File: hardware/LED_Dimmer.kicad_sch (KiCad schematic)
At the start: 11 parts, among them J1 Molex PicoBlade 53261-0871 1x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, Q1 2N7002K-7, Q2 2N7002K-7, Q3 2N7002K-7, U1 BGM220P, U2 L78L33A

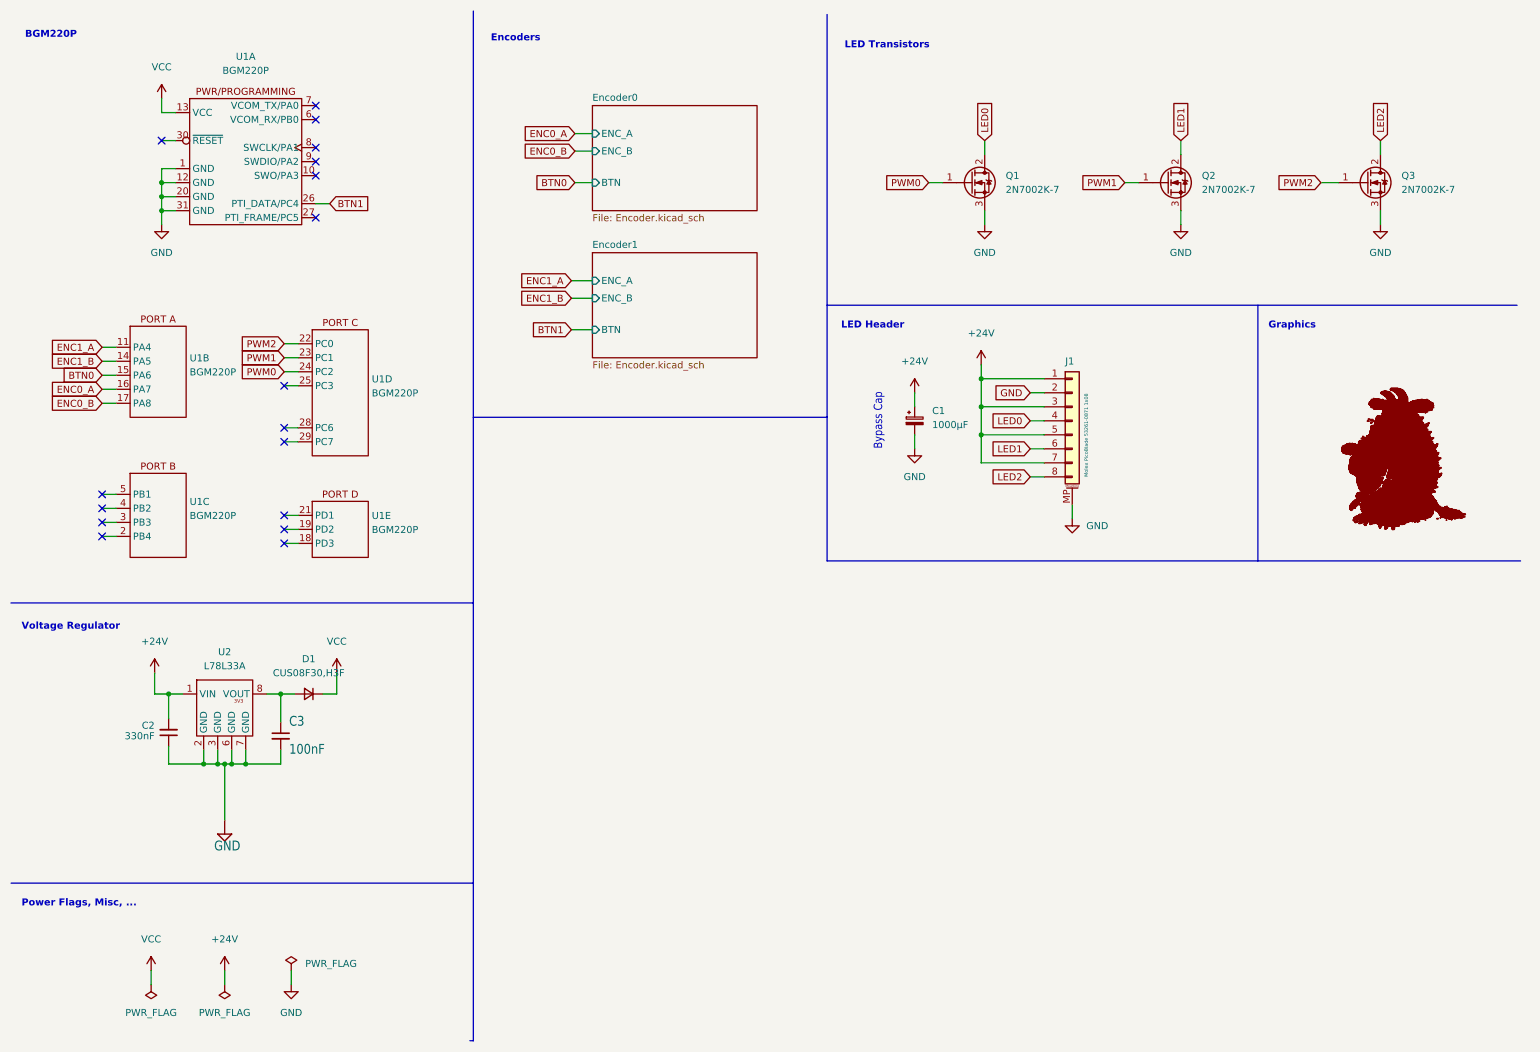
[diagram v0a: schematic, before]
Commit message: v2 Board Ready - Added Art - Removed DRC/ERC - Finished BOM
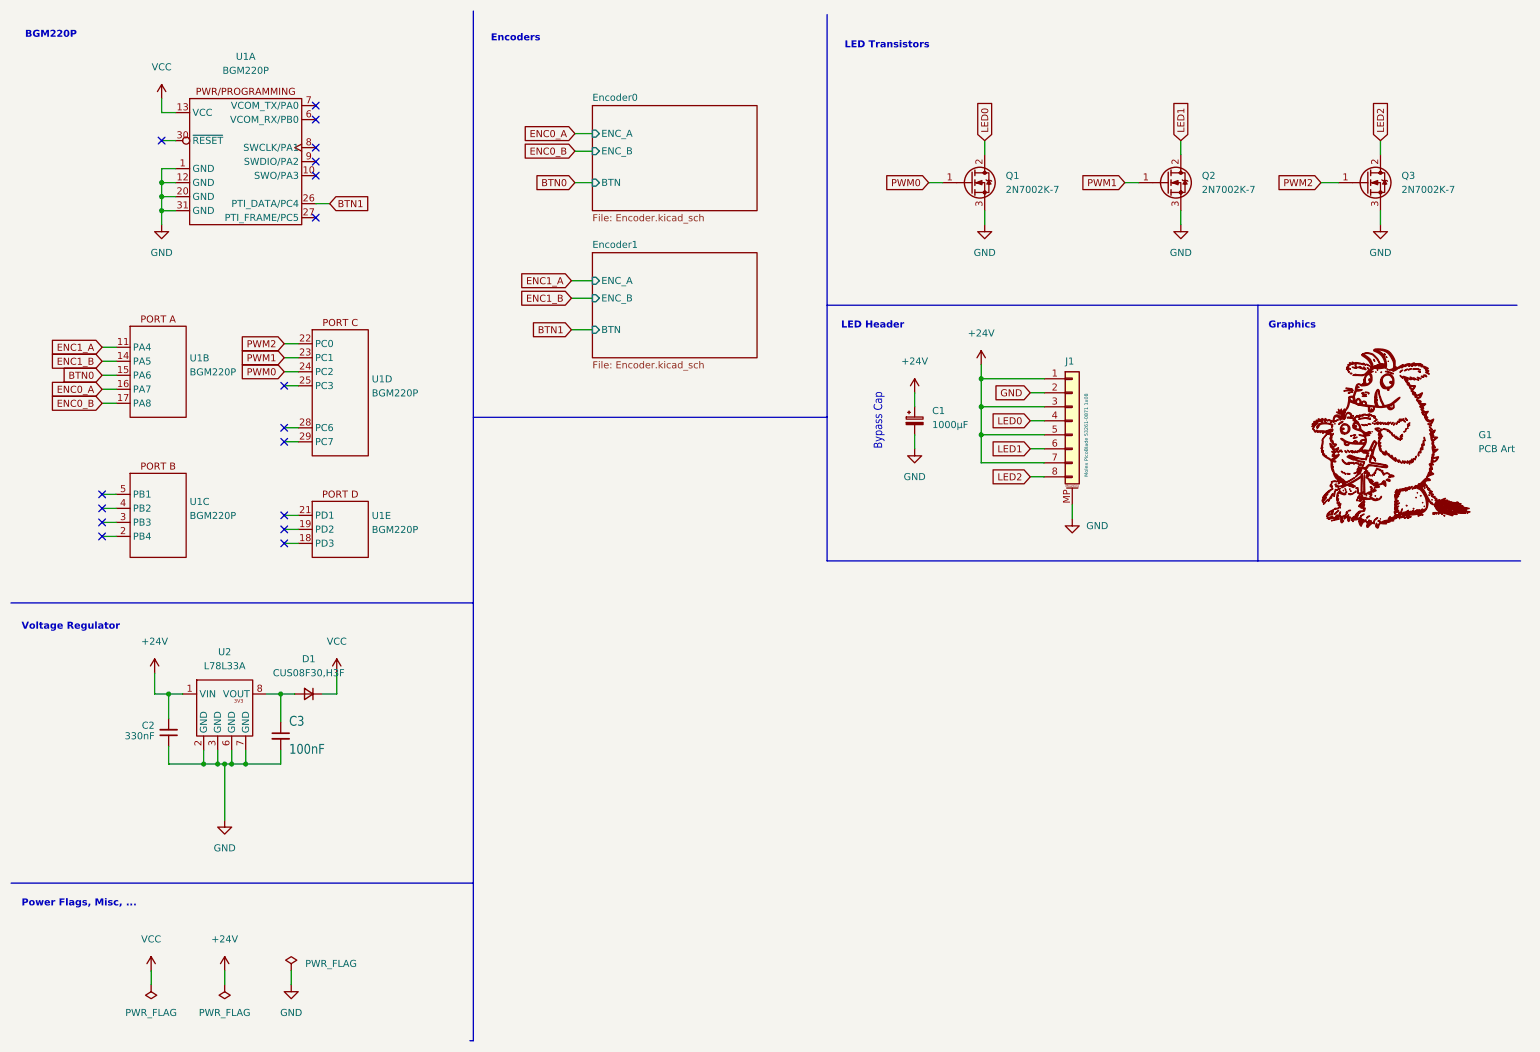
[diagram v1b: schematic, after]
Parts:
- removed G1: GRUFFALO, LED_Dimmer:GRUFFALO, symbol LED_Dimmer-eagle-import:GRUFFALO
- added G1: PCB Art, Gruffalo_Dimmer:Gruffalo_Art, symbol Gruffalo_Dimmer:PCB Art
- C3: Comments (none) -> Any X7R, 0603, 10V cap. Farnell MPN is alternative; Digikey PN (none) -> 1276-1935-1-ND; Farnell PN (none) -> 1362556; MPN (none) -> CL10B104KB8NNWC; Manufacturer (none) -> Samsung; Tolerance (none) -> X7R; Vrating (none) -> 50V

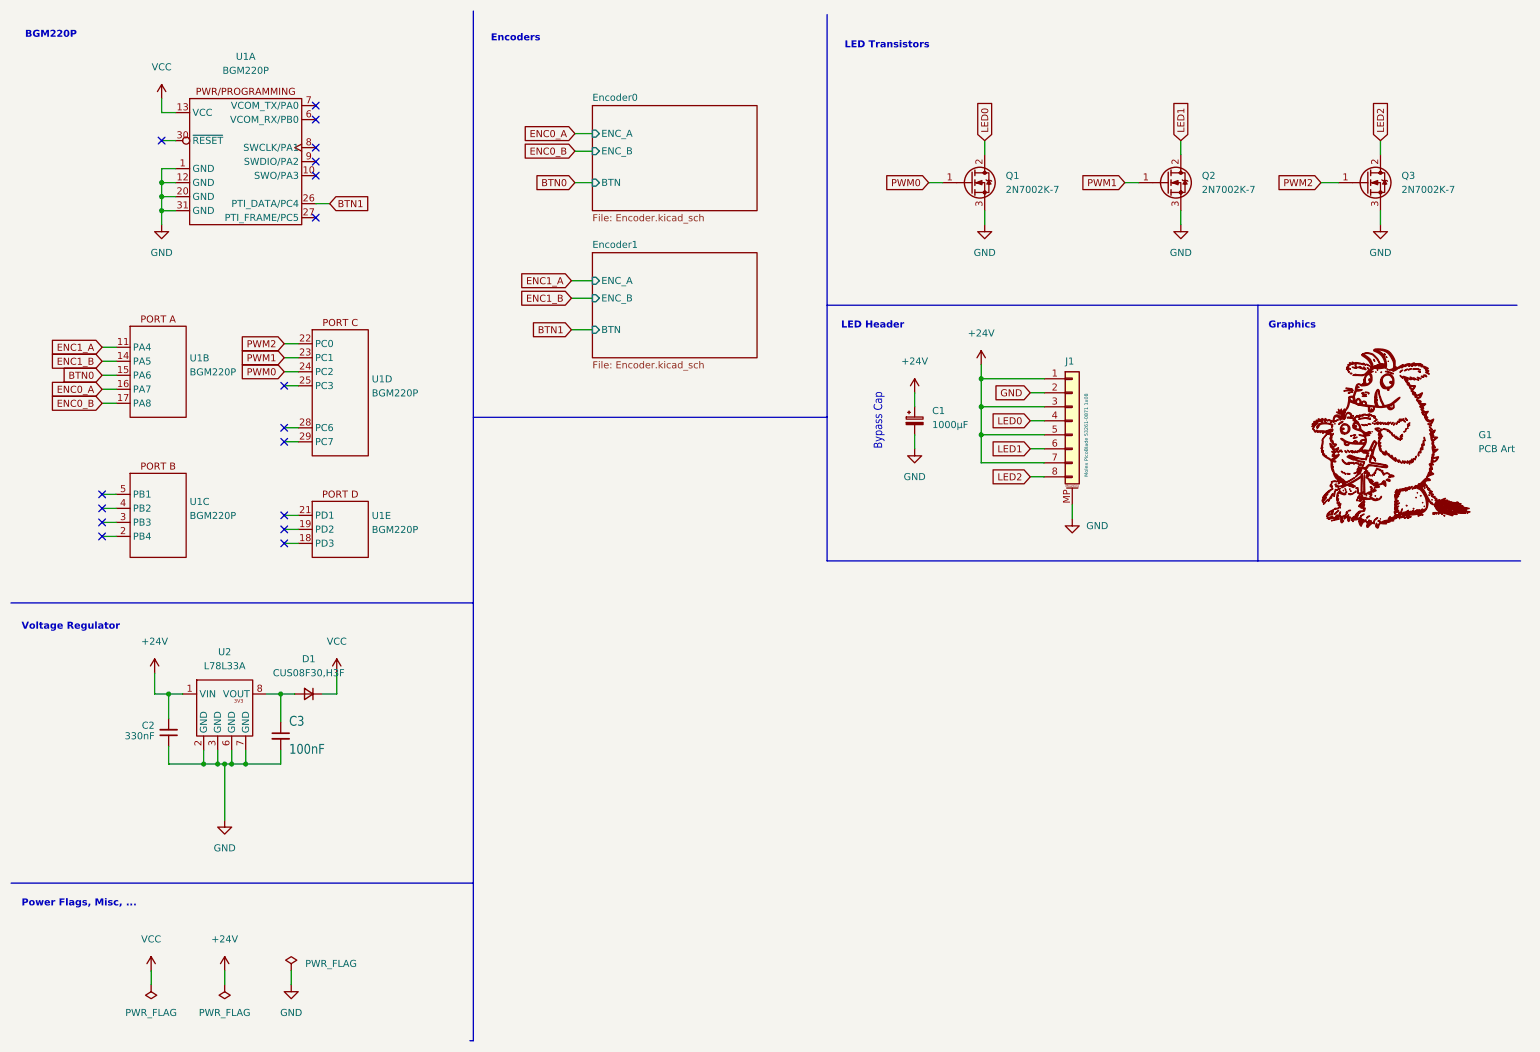
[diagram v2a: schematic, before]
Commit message: Not sure of the complete list of changes, but fixed a bunch of DRC/ERC errors
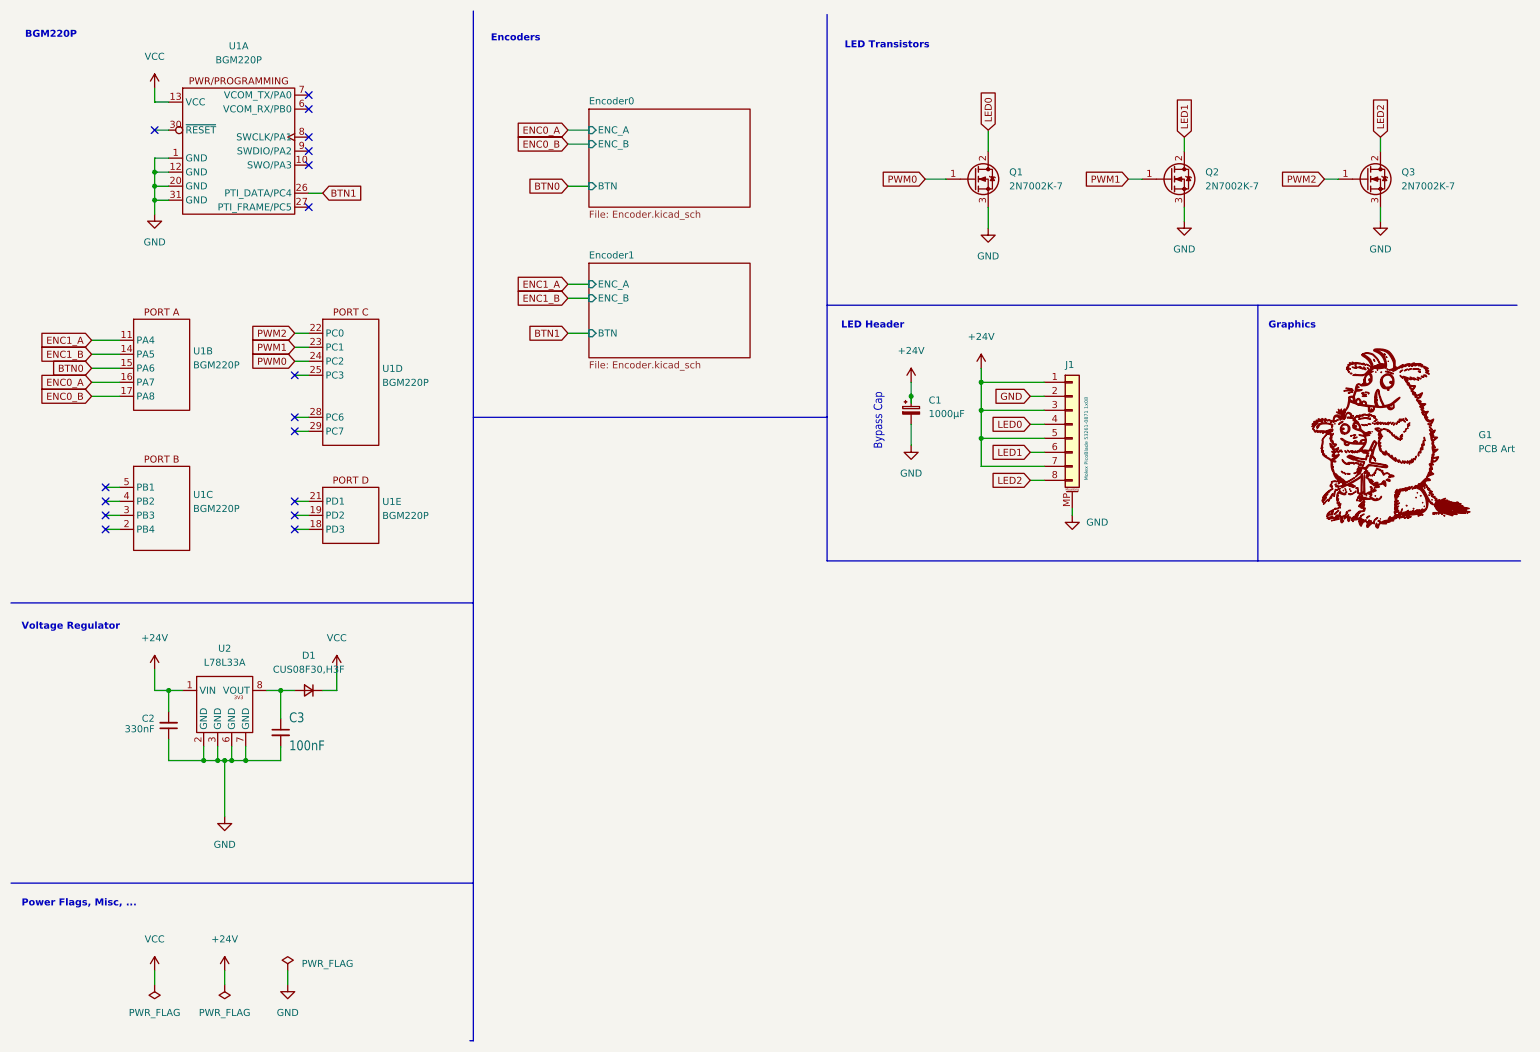
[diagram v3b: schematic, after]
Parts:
- G1: now left out of the parts list
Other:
- moved on the sheet: C1, C2, C3, D1, J1, Q1, Q2, Q3, U1A, U1B, U1C, U1D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

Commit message: Changed a digikey PN and removed the gruffalo art from the BOM
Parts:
- U2: Digikey PN L78L33ACD-ND -> 497-1199-1-ND
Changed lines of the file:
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@@
       (effects (font (size 1.27 1.27)) hide)
     )
-    (property "Digikey PN" "L78L33ACD-ND" (at 50.8 137.16 0)
+    (property "Digikey PN" "497-1199-1-ND" (at 50.8 137.16 0)
       (effects (font (size 1.27 1.27)) hide)
     )
@@
   (symbol (lib_id "Gruffalo_Dimmer:PCB Art") (at 262.255 88.9 0) (unit 1)
     (in_bom no) (on_board yes) (dnp no) (fields_autoplaced)
-    (property "Reference" "G1" (at 278.13 88.2783 0)
-      (effects (font (size 1.27 1.27)) (justify left))
-    )
-    (property "Value" "PCB Art" (at 278.13 90.8183 0)
-      (effects (font (size 1.27 1.27)) (justify left))
-    )
+    (property "Reference" "G1" (at 278.13 87.6433 0)
+      (effects (font (size 1.27 1.27)) (justify left))
+    )
+    (property "Value" "PCB Art" (at 278.13 90.1833 0)
+      (effects (font (size 1.27 1.27)) (justify left))
+    )

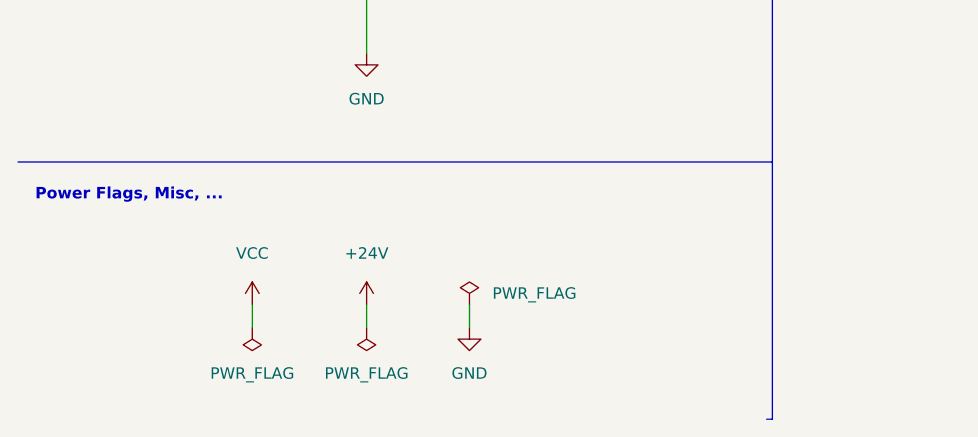
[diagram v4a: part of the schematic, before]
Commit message: Added some parts to the BoM that are not on the board (connector receptacle, crimps) Checked status of MPNs, and removed some old ones
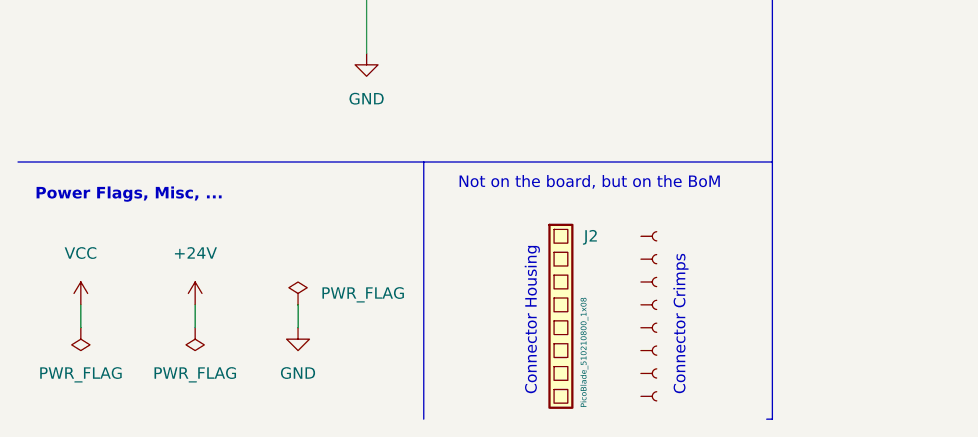
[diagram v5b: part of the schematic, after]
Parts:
- added J2: PicoBlade_510210800_1x08, symbol Gruffalo_Dimmer:PicoBlade_Housing_510210800_1x08
- added M1, M2, M3, M4, M5, M6, M7, M8: 500798001, symbol Gruffalo_Dimmer:PicoBlade_Crimp_500798001_1x01
- U2: Digikey PN 497-1199-1-ND -> 497-7285-1-ND; MPN L78L33ACD13TR -> L78L33ABD
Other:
- note added: "Connector Crimps"
- note added: "Connector Housing"
- note added: "Not on the board, but on the BoM"
